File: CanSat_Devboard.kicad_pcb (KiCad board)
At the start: 6 copper layers, 0 parts

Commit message: Finished preliminary project schematics and architecture
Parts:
- added BT1: 1S Lipo, Connector_JST:JST_XH_B2B-XH-A_1x02_P2.50mm_Vertical, F.Cu at (72.5, 126.9)
- added C1: 22p, Capacitor_SMD:C_0603_1608Metric, F.Cu at (82.5, 124.7)
- added C10: 10u, Capacitor_SMD:C_0603_1608Metric, F.Cu at (63.0, 127.2)
- added C11: 10u, Capacitor_SMD:C_0603_1608Metric, F.Cu at (63.0, 129.8)
- added C2: 22p, Capacitor_SMD:C_0603_1608Metric, F.Cu at (82.5, 127.2)
- added C3: 10u, Capacitor_SMD:C_0603_1608Metric, F.Cu at (59.0, 124.7)
- added C4: 0.1u, Capacitor_SMD:C_0603_1608Metric, F.Cu at (59.0, 127.2)
- added C5: 1u, Capacitor_SMD:C_0603_1608Metric, F.Cu at (59.0, 129.8)
- added C6: 10u, Capacitor_SMD:C_0603_1608Metric, F.Cu at (59.0, 132.3)
- added C7: 10u, Capacitor_SMD:C_0603_1608Metric, F.Cu at (59.0, 134.8)
- added C8: 1u, Capacitor_SMD:C_0603_1608Metric, F.Cu at (59.0, 137.3)
- added C9: 2u2, Capacitor_SMD:C_0603_1608Metric, F.Cu at (63.0, 124.7)
- added D1: Amber, LED_SMD:LED_0603_1608Metric, F.Cu at (71.1, 132.6)
- added D2: Amber, LED_SMD:LED_0603_1608Metric, F.Cu at (71.1, 135.2)
- added D3: Amber, LED_SMD:LED_0603_1608Metric, F.Cu at (71.1, 137.8)
- added FB1: LI0603G121R-10, Inductor_SMD:L_0603_1608Metric, F.Cu at (83.7, 156.4)
- added IC1: 114993390, 00_lora:wio-sx1262, F.Cu at (126.7, 119.2)
- added J1: USB_C_Receptacle_USB2.0_16P, Connector_USB:USB_C_Receptacle_GCT_USB4105-xx-A_16P_TopMnt_Horizontal, F.Cu at (81.7, 150.5)
- added J2: SWD, Connector_PinHeader_2.54mm:PinHeader_2x03_P2.54mm_Vertical, F.Cu at (59.3, 147.5)
- added J3: RMF, Connector_PinHeader_2.54mm:PinHeader_1x02_P2.54mm_Vertical, F.Cu at (66.4, 156.8)
- added L1: 10u(DNP), Inductor_SMD:L_Changjiang_FTC201610D, F.Cu at (86.3, 125.1)
- added L2: 2u2, Inductor_SMD:L_0805_2012Metric_Pad1.05x1.20mm_HandSolder, F.Cu at (75.5, 132.7)
- added L3: 2u2, Inductor_SMD:L_0805_2012Metric_Pad1.05x1.20mm_HandSolder, F.Cu at (75.5, 135.4)
- added NT1: NetTie_2, NetTie:NetTie-2_SMD_Pad0.5mm, F.Cu at (74.3, 137.5)
- added NT2: NetTie_2, NetTie:NetTie-2_SMD_Pad0.5mm, F.Cu at (74.3, 139.0)
- added R1: 4k7, Resistor_SMD:R_0603_1608Metric, F.Cu at (63.0, 132.3)
- added R2: 4k7, Resistor_SMD:R_0603_1608Metric, F.Cu at (63.0, 134.8)
- added R3: 150k, Resistor_SMD:R_0603_1608Metric, F.Cu at (63.0, 137.3)
- added R4: 47k, Resistor_SMD:R_0603_1608Metric, F.Cu at (67.0, 124.7)
- added R5: 300, Resistor_SMD:R_0603_1608Metric, F.Cu at (67.0, 127.2)
- added R6: 300, Resistor_SMD:R_0603_1608Metric, F.Cu at (67.0, 129.8)
- added R7: 300, Resistor_SMD:R_0603_1608Metric, F.Cu at (67.0, 132.3)
- added SW1: SHPHLD, Button_Switch_SMD:SW_Push_1P1T_NO_CK_KMR2, F.Cu at (60.3, 140.9)
- added SW2: SW_Push, Button_Switch_SMD:SW_Push_1P1T_NO_CK_KMR2, F.Cu at (67.5, 147.5)
- added SW3: RST, Button_Switch_SMD:SW_Push_1P1T_NO_CK_KMR2, F.Cu at (67.5, 152.2)
- added TP1: VMCU, TestPoint:TestPoint_Pad_D1.0mm, F.Cu at (72.3, 146.7)
- added TP2: 3V3, TestPoint:TestPoint_Pad_D1.0mm, F.Cu at (72.3, 149.8)
- added TP3: VSYS, TestPoint:TestPoint_Pad_D1.0mm, F.Cu at (72.3, 152.8)
- added U1: E73-2G4M08S1C, E73-2G4M08S1C:E73-2G4M08S1C, F.Cu at (143.0, 118.8)
- added U2: SRV05-4, Package_TO_SOT_SMD:SOT-23-6_Handsoldering, F.Cu at (78.8, 157.6)

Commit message: Edited ci.yaml
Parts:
- added C12: 0.1u, Capacitor_SMD:C_0603_1608Metric_Pad1.08x0.95mm_HandSolder, F.Cu at (189.8, 130.4)
- added C13: 10u, Capacitor_SMD:C_0603_1608Metric_Pad1.08x0.95mm_HandSolder, F.Cu at (189.8, 132.9)
- added R10: 47k, Resistor_SMD:R_1206_3216Metric_Pad1.30x1.75mm_HandSolder, F.Cu at (184.6, 137.4)
- added R8: 47k, Resistor_SMD:R_1206_3216Metric_Pad1.30x1.75mm_HandSolder, F.Cu at (184.6, 130.8)
- added R9: 47k, Resistor_SMD:R_1206_3216Metric_Pad1.30x1.75mm_HandSolder, F.Cu at (184.6, 134.1)
- added U4: RAK3172, Project_Components:XCVR_RAK3172, F.Cu at (191.6, 117.8)
- NT1, NT2: footprint NetTie:NetTie-2_SMD_Pad0.5mm -> NetTie:NetTie-2_SMD_Pad2.0mm
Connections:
- net RMF renamed /Project Architecture/Misc/RMF

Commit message: Cleaned up
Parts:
- removed BT1: 1S Lipo, Connector_JST:JST_XH_B2B-XH-A_1x02_P2.50mm_Vertical
- removed C1, C2: 22p, Capacitor_SMD:C_0603_1608Metric
- removed C10, C11, C3, C6, C7: 10u, Capacitor_SMD:C_0603_1608Metric
- removed C12: 0.1u, Capacitor_SMD:C_0603_1608Metric_Pad1.08x0.95mm_HandSolder
- removed C13: 10u, Capacitor_SMD:C_0603_1608Metric_Pad1.08x0.95mm_HandSolder
- removed C4: 0.1u, Capacitor_SMD:C_0603_1608Metric
- removed C5, C8: 1u, Capacitor_SMD:C_0603_1608Metric
- removed C9: 2u2, Capacitor_SMD:C_0603_1608Metric
- removed D1, D2, D3: Amber, LED_SMD:LED_0603_1608Metric
- removed FB1: LI0603G121R-10, Inductor_SMD:L_0603_1608Metric
- removed IC1: 114993390, 00_lora:wio-sx1262
- removed J1: USB_C_Receptacle_USB2.0_16P, Connector_USB:USB_C_Receptacle_GCT_USB4105-xx-A_16P_TopMnt_Horizontal
- removed J2: SWD, Connector_PinHeader_2.54mm:PinHeader_2x03_P2.54mm_Vertical
- removed J3: RMF, Connector_PinHeader_2.54mm:PinHeader_1x02_P2.54mm_Vertical
- removed L1: 10u(DNP), Inductor_SMD:L_Changjiang_FTC201610D
- removed L2, L3: 2u2, Inductor_SMD:L_0805_2012Metric_Pad1.05x1.20mm_HandSolder
- removed NT1, NT2: NetTie_2, NetTie:NetTie-2_SMD_Pad2.0mm
- removed R1, R2: 4k7, Resistor_SMD:R_0603_1608Metric
- removed R10, R8, R9: 47k, Resistor_SMD:R_1206_3216Metric_Pad1.30x1.75mm_HandSolder
- removed R3: 150k, Resistor_SMD:R_0603_1608Metric
- removed R4: 47k, Resistor_SMD:R_0603_1608Metric
- removed R5, R6, R7: 300, Resistor_SMD:R_0603_1608Metric
- removed SW1: SHPHLD, Button_Switch_SMD:SW_Push_1P1T_NO_CK_KMR2
- removed SW2: SW_Push, Button_Switch_SMD:SW_Push_1P1T_NO_CK_KMR2
- removed SW3: RST, Button_Switch_SMD:SW_Push_1P1T_NO_CK_KMR2
- removed TP1: VMCU, TestPoint:TestPoint_Pad_D1.0mm
- removed TP2: 3V3, TestPoint:TestPoint_Pad_D1.0mm
- removed TP3: VSYS, TestPoint:TestPoint_Pad_D1.0mm
- removed U1: E73-2G4M08S1C, E73-2G4M08S1C:E73-2G4M08S1C
- removed U2: SRV05-4, Package_TO_SOT_SMD:SOT-23-6_Handsoldering
- removed U4: RAK3172, Project_Components:XCVR_RAK3172

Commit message: Updated layout with the footprints
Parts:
- added BT1: 1S Lipo, Connector_JST:JST_XH_B2B-XH-A_1x02_P2.50mm_Vertical, F.Cu at (163.9, 83.6)
- added C1: 22p, Capacitor_SMD:C_0603_1608Metric, F.Cu at (122.5, 92.4)
- added C11: 1u, Capacitor_SMD:C_0603_1608Metric, F.Cu at (117.4, 99.4)
- added C12: 1u, Capacitor_SMD:C_0603_1608Metric, F.Cu at (117.4, 101.9)
- added C13: 2u2, Capacitor_SMD:C_0603_1608Metric, F.Cu at (117.4, 104.4)
- added C14: 10u, Capacitor_SMD:C_0603_1608Metric, F.Cu at (117.4, 106.9)
- added C15: 0.1u, Capacitor_SMD:C_0603_1608Metric, F.Cu at (117.4, 109.4)
- added C16: 10u, Capacitor_SMD:C_0603_1608Metric, F.Cu at (117.4, 112.0)
- added C17: 10u, Capacitor_SMD:C_0603_1608Metric, F.Cu at (121.4, 99.4)
- added C18: 10u, Capacitor_SMD:C_0603_1608Metric, F.Cu at (121.4, 101.9)
- added C19: 10u, Capacitor_SMD:C_0603_1608Metric, F.Cu at (121.4, 104.4)
- added C2: 22p, Capacitor_SMD:C_0603_1608Metric, F.Cu at (122.5, 94.9)
- added C3: 0.1u, Capacitor_SMD:C_0603_1608Metric, F.Cu at (154.9, 99.4)
- added C4: 10u, Capacitor_SMD:C_0603_1608Metric, F.Cu at (154.9, 101.9)
- added D4: Amber, LED_SMD:LED_0603_1608Metric, F.Cu at (129.4, 99.4)
- added D5: Green, LED_SMD:LED_0603_1608Metric, F.Cu at (129.4, 102.0)
- added D6: Blue, LED_SMD:LED_0603_1608Metric, F.Cu at (129.4, 104.6)
- added FB1: LI0603G121R-10, Inductor_SMD:L_0603_1608Metric, F.Cu at (166.8, 127.7)
- added IC1: 114993390, Project_Components:114993390, F.Cu at (166.3, 106.3)
- added J2: SWD, Connector_PinHeader_2.54mm:PinHeader_2x03_P2.54mm_Vertical, F.Cu at (162.7, 72.9)
- added J3: RMF, Connector_PinHeader_2.54mm:PinHeader_1x02_P2.54mm_Vertical, F.Cu at (172.1, 82.5)
- added J4: USB_C_Receptacle_USB2.0_16P, Connector_USB:USB_C_Receptacle_GCT_USB4105-xx-A_16P_TopMnt_Horizontal, F.Cu at (164.8, 121.7)
- added J5: 693071010811, Project_Components:693071010811, F.Cu at (144.9, 106.8)
- added L1: 10u(DNP), Inductor_SMD:L_Changjiang_FTC201610D, F.Cu at (126.3, 92.8)
- added L4: 2u2, Inductor_SMD:L_0805_2012Metric_Pad1.05x1.20mm_HandSolder, F.Cu at (124.8, 114.6)
- added L5: 2u2, Inductor_SMD:L_0805_2012Metric_Pad1.05x1.20mm_HandSolder, F.Cu at (124.8, 117.3)
- added NT1: NetTie_2, NetTie:NetTie-2_SMD_Pad2.0mm, F.Cu at (118.8, 114.7)
- added NT2: NetTie_2, NetTie:NetTie-2_SMD_Pad2.0mm, F.Cu at (118.8, 117.7)
- added R1: 47k, Resistor_SMD:R_0603_1608Metric, F.Cu at (154.9, 104.4)
- added R11: 4k7, Resistor_SMD:R_0603_1608Metric, F.Cu at (121.4, 106.9)
- added R12: 4k7, Resistor_SMD:R_0603_1608Metric, F.Cu at (121.4, 109.4)
- added R13: 310, Resistor_SMD:R_0603_1608Metric, F.Cu at (121.4, 112.0)
- added R14: 180, Resistor_SMD:R_0603_1608Metric, F.Cu at (125.4, 99.4)
- added R15: 180, Resistor_SMD:R_0603_1608Metric, F.Cu at (125.4, 101.9)
- added R16: 150k, Resistor_SMD:R_0603_1608Metric, F.Cu at (125.4, 104.4)
- added R17: 47k, Resistor_SMD:R_0603_1608Metric, F.Cu at (125.4, 106.9)
- added R2: 47k, Resistor_SMD:R_0603_1608Metric, F.Cu at (154.9, 106.9)
- added R3: 47k, Resistor_SMD:R_0603_1608Metric, F.Cu at (154.9, 109.4)
- added SW1: SW_Push, Button_Switch_SMD:SW_Push_1P1T_NO_CK_KMR2, F.Cu at (170.9, 72.9)
- added SW2: RST, Button_Switch_SMD:SW_Push_1P1T_NO_CK_KMR2, F.Cu at (170.9, 77.5)
- added SW4: SHPHLD, Button_Switch_SMD:SW_Push_1P1T_NO_CK_KMR2, F.Cu at (130.7, 115.9)
- added TP1: VMCU, TestPoint:TestPoint_Pad_D1.0mm, F.Cu at (158.9, 72.1)
- added TP2: 3V3, TestPoint:TestPoint_Pad_D1.0mm, F.Cu at (158.9, 75.1)
- added TP3: VSYS, TestPoint:TestPoint_Pad_D1.0mm, F.Cu at (158.9, 78.2)
- added TP4: VLDO, TestPoint:TestPoint_Pad_D1.0mm, F.Cu at (158.9, 81.2)
- added TP5: CC1, TestPoint:TestPoint_Pad_D1.0mm, F.Cu at (172.2, 118.0)
- added TP6: CC2, TestPoint:TestPoint_Pad_D1.0mm, F.Cu at (172.2, 121.0)
- added U1: E73-2G4M08S1C, E73-2G4M08S1C:E73-2G4M08S1C, F.Cu at (135.3, 80.6)
- added U3: SRV05-4, Package_TO_SOT_SMD:SOT-23-6_Handsoldering, F.Cu at (161.9, 128.9)
- added U4: NPM1300-QEAA-R7, Project_Components:QFN32_5X5_NOR, F.Cu at (131.0, 109.7)
- added Y1: 32.768, Project_Components:WE-XTAL_CFPX-217, F.Cu at (117.9, 92.8)

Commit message: Started PCB layout
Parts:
- added J1: I2C, Connector_PinHeader_2.54mm:PinHeader_1x04_P2.54mm_Vertical, F.Cu at (110.1, 87.4)
- added J3: Conn_01x03_Pin, Connector_JST:JST_XH_B3B-XH-A_1x03_P2.50mm_Vertical, F.Cu at (100.0, 103.2)
- added J6: SWD, Connector_PinHeader_2.54mm:PinHeader_2x03_P2.54mm_Vertical, F.Cu at (95.8, 80.3)
- added J7: RMF, Connector_PinHeader_2.54mm:PinHeader_1x02_P2.54mm_Vertical, F.Cu at (110.1, 80.3)
- added J8: GPIO, Connector_PinHeader_2.54mm:PinHeader_2x07_P2.54mm_Vertical, F.Cu at (102.9, 80.3)
- added SW3: SW_Push, Button_Switch_SMD:SW_Push_1P1T_NO_CK_KMR2, F.Cu at (96.8, 90.0)
- added SW5: RST, Button_Switch_SMD:SW_Push_1P1T_NO_CK_KMR2, F.Cu at (96.8, 94.6)
- added TP10: VLDO, TestPoint:TestPoint_Pad_D1.0mm, F.Cu at (95.0, 110.5)
- added TP7: VMCU, TestPoint:TestPoint_Pad_D1.0mm, F.Cu at (95.0, 101.4)
- added TP8: VSYS, TestPoint:TestPoint_Pad_D1.0mm, F.Cu at (95.0, 104.4)
- added TP9: 3V3, TestPoint:TestPoint_Pad_D1.0mm, F.Cu at (95.0, 107.5)
- L1: footprint Inductor_SMD:L_Changjiang_FTC201610D -> Inductor_SMD:L_1210_3225Metric
- L4, L5: footprint Inductor_SMD:L_0805_2012Metric_Pad1.05x1.20mm_HandSolder -> Inductor_SMD:L_1812_4532Metric
- NT1, NT2: footprint NetTie:NetTie-2_SMD_Pad2.0mm -> Project_Components:Net_tie_1mm
- moved IC1 53.3 mm to (119.4, 81.0)
- moved J4 47.0 mm to (150.5, 77.0), turned to 180 degrees
- moved U3 46.5 mm to (148.0, 84.5)
- moved TP5 30.7 mm to (159.5, 90.0)
- moved TP6 30.3 mm to (159.5, 93.5)
- moved U4 26.8 mm to (151.5, 92.5)
- moved J5 2.37 mm to (144.0, 109.0)
- moved L5 1.67 mm to (124.8, 119.0)
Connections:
- J5 pad 6: unconnected-(J5-VSS-Pad6) -> GND
- U1 pad 10: /Project Architecture/Misc/RMF -> RMF
- U3 pad 5: +5V -> VBUS
- U4 pad 18: GND -> NTC
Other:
- copper layers 6 -> 4

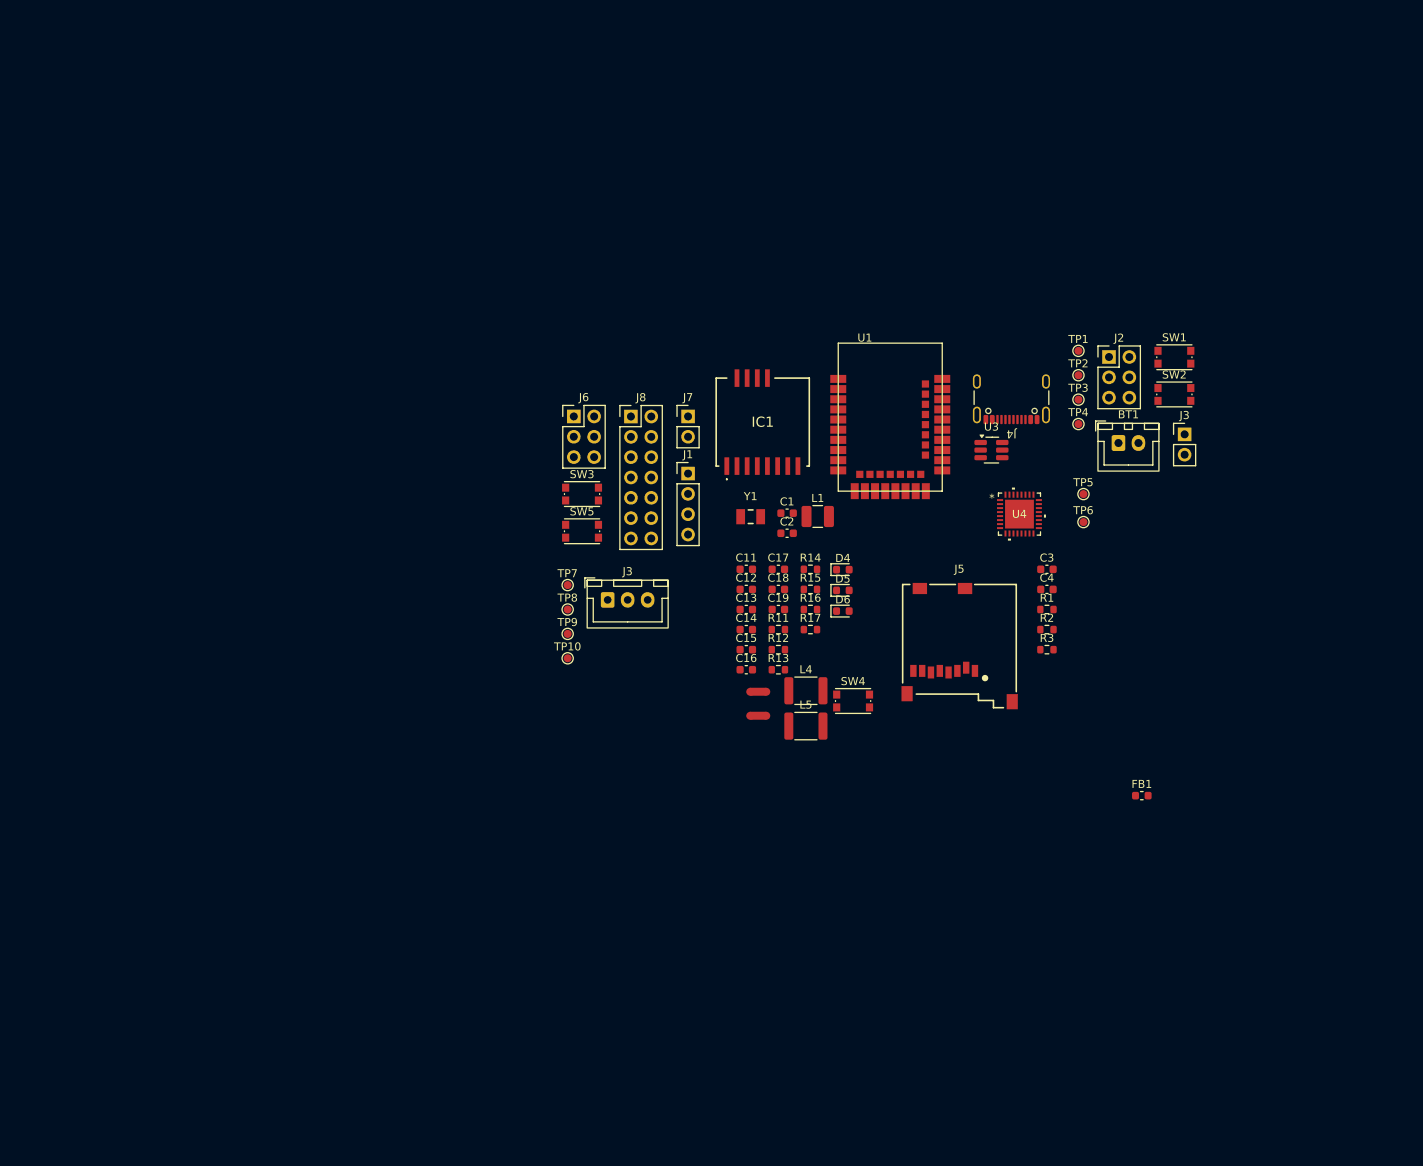
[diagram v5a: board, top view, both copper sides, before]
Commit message: Started layout
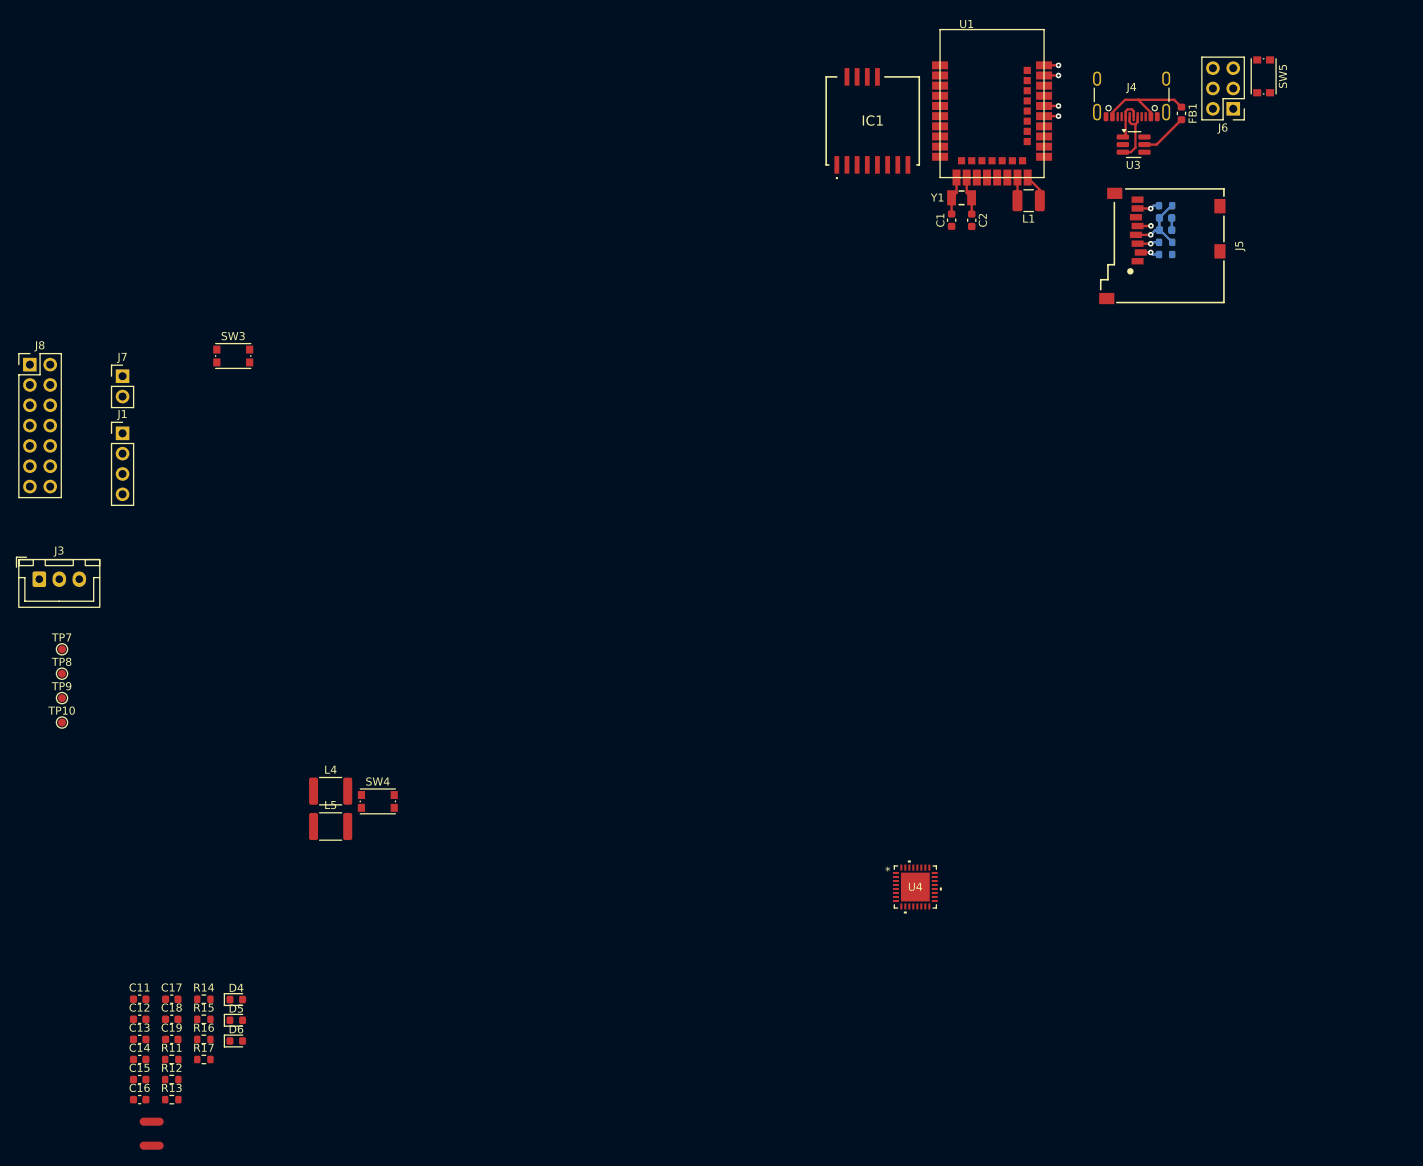
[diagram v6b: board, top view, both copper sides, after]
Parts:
- removed BT1: 1S Lipo, Connector_JST:JST_XH_B2B-XH-A_1x02_P2.50mm_Vertical
- removed J2: SWD, Connector_PinHeader_2.54mm:PinHeader_2x03_P2.54mm_Vertical
- removed the J3 at (172.1, 82.5)
- removed SW1: SW_Push, Button_Switch_SMD:SW_Push_1P1T_NO_CK_KMR2
- removed SW2: RST, Button_Switch_SMD:SW_Push_1P1T_NO_CK_KMR2
- removed TP1: VMCU, TestPoint:TestPoint_Pad_D1.0mm
- removed TP2: 3V3, TestPoint:TestPoint_Pad_D1.0mm
- removed TP3: VSYS, TestPoint:TestPoint_Pad_D1.0mm
- removed TP4: VLDO, TestPoint:TestPoint_Pad_D1.0mm
- removed TP5: CC1, TestPoint:TestPoint_Pad_D1.0mm
- removed TP6: CC2, TestPoint:TestPoint_Pad_D1.0mm
- C3, C4, R1, R2, R3: moved to B.Cu
- moved SW5 102.4 mm to (182.0, 37.8), turned to -90 degrees
- moved C11 92.9 mm to (41.5, 153.1)
- moved C12 92.9 mm to (41.5, 155.7)
- moved C13 92.9 mm to (41.5, 158.2)
- moved C15 92.9 mm to (41.5, 163.2)
- moved C16 92.9 mm to (41.5, 165.7)
- moved C17 92.9 mm to (45.5, 153.1)
- moved C18 92.9 mm to (45.5, 155.7)
- moved C19 92.9 mm to (45.5, 158.2)
- moved NT1 92.9 mm to (43.0, 168.4)
- moved NT2 92.9 mm to (43.0, 171.4)
- moved R12 92.9 mm to (45.5, 163.2)
- moved R13 92.9 mm to (45.5, 165.7)
- moved C14 92.9 mm to (41.5, 160.7)
- moved D4 92.9 mm to (53.6, 153.2)
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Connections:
- U1 pad 33: unconnected-(U1B-P0.13-Pad33) -> CS
- U1 pad 35: unconnected-(U1B-P0.24-Pad35) -> MOSI
- U1 pad 36: CS -> unconnected-(U1C-P1.00-Pad36)
- U1 pad 38: MOSI -> unconnected-(U1C-P1.02-Pad38)
- U1 pad 40: SCK -> unconnected-(U1C-P1.04-Pad40)
- U1 pad 41: unconnected-(U1B-P0.09/NFC1-Pad41) -> SCK
- U1 pad 42: MISO -> unconnected-(U1C-P1.06-Pad42)
- U1 pad 43: unconnected-(U1B-P0.10/NFC2-Pad43) -> MISO
- U3 pad 3: unconnected-(U3-IO2-Pad3) -> /Project Architecture/OBC/D-
- U3 pad 6: /Project Architecture/OBC/D- -> unconnected-(U3-IO4-Pad6)
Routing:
- net Net-(FB1-Pad1): track 0.00 -> 13.0 mm
- net +3.3V: track 0.00 -> 9.18 mm, vias 0 -> 1
- net /Project Architecture/OBC/D-: track 0.00 -> 7.31 mm
- net VBUS: track 0.00 -> 5.91 mm
- net /Project Architecture/OBC/D+: track 0.00 -> 5.24 mm
- net Net-(U1B-P0.01/XL2): track 0.00 -> 4.82 mm
- net Net-(U1B-P0.00/XL1): track 0.00 -> 4.81 mm
- net MISO: track 0.00 -> 4.64 mm, vias 0 -> 2
- net MOSI: track 0.00 -> 4.58 mm, vias 0 -> 2
- net CS: track 0.00 -> 4.19 mm, vias 0 -> 2
- net Net-(U1A-DCCH): track 0.00 -> 3.52 mm
- net SCK: track 0.00 -> 3.49 mm, vias 0 -> 2
- net VMCU: track 0.00 -> 2.89 mm
- net GND: track 0.00 -> 1.52 mm
